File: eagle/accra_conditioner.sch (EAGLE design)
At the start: 25 parts, among them T1 PT204-6C, X1 WIREPAD1,6/0,8, X10 WIREPAD1,6/0,8, X11 WIREPAD1,6/0,8, X12 WIREPAD1,6/0,8, X13 WIREPAD1,6/0,8, X14 WIREPAD1,6/0,8, X15 WIREPAD1,6/0,8, X16 WIREPAD1,6/0,8, X2 WIREPAD1,6/0,8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

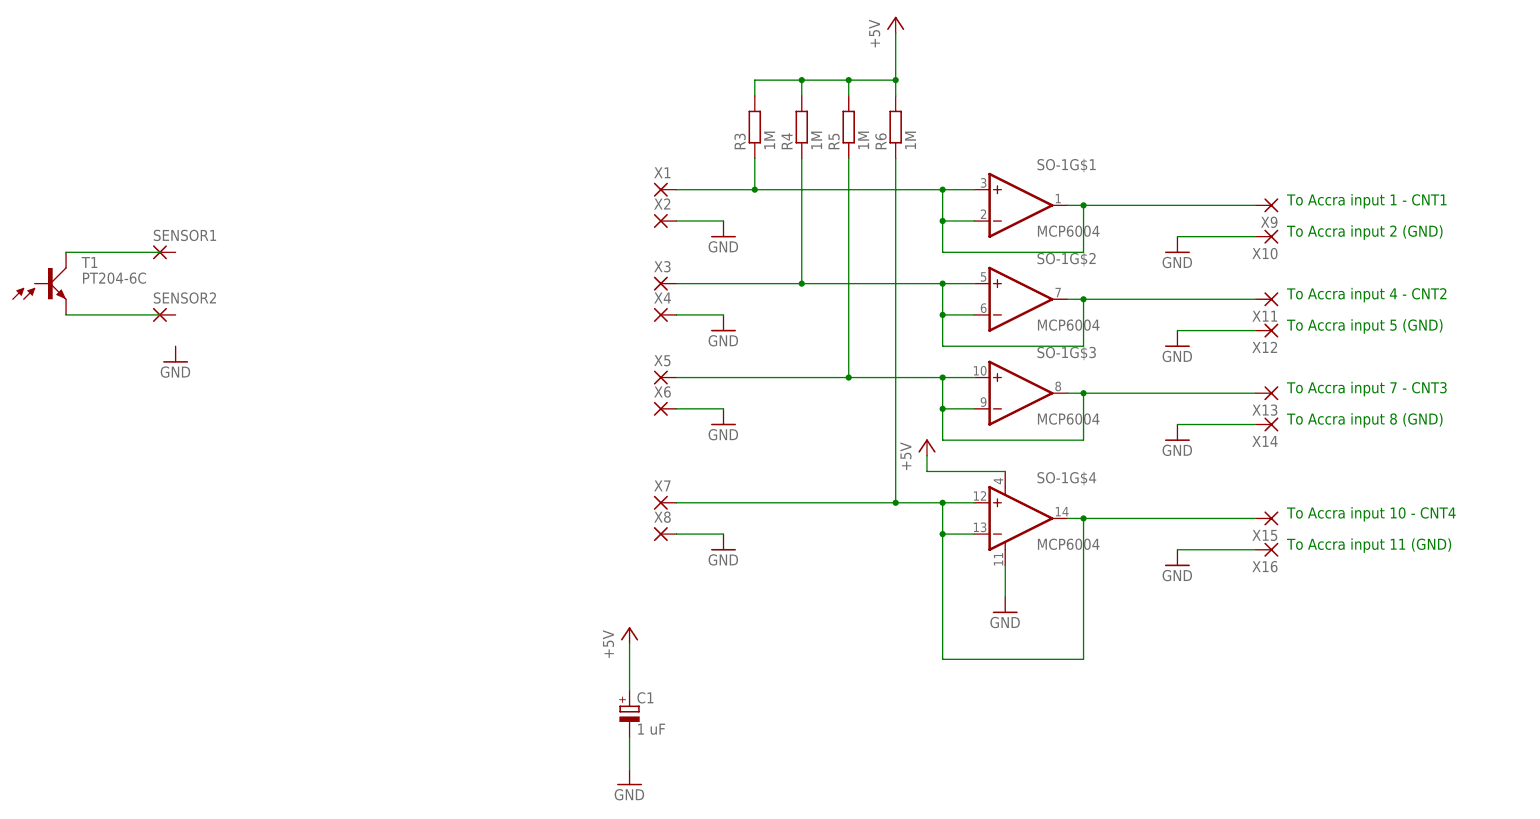
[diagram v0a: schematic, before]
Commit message: Fixed buffer amp.
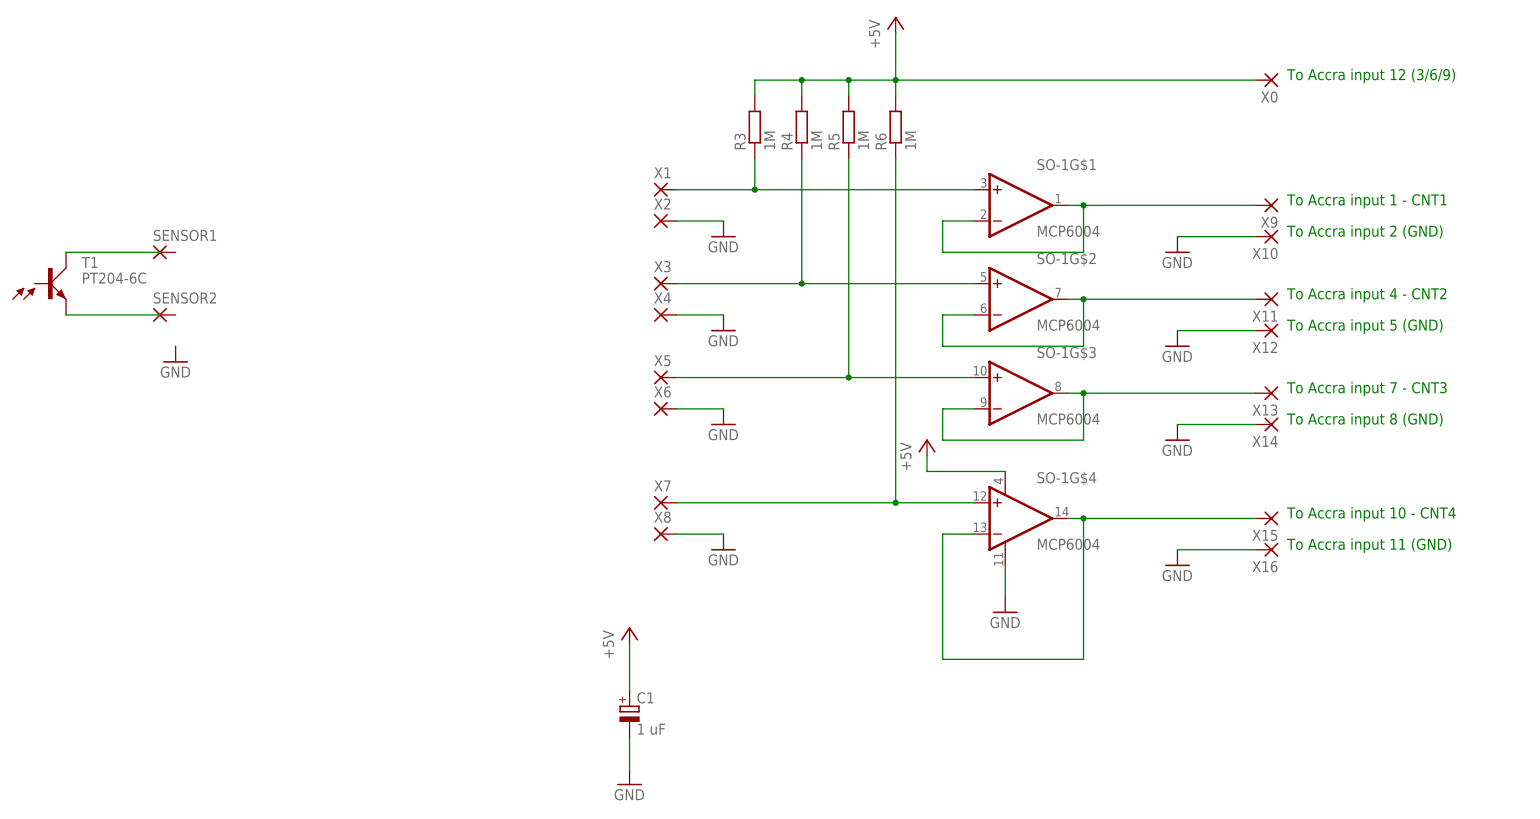
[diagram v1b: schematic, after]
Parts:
- added X0: WIREPAD1,6/0,8, wirepad:WIREPAD1,6/0,8
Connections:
- new net N$10: SO-1G$4.-IN, SO-1G$4.OUT, X15.P
- new net N$2: R3.1, SO-1G$1.+IN, X1.P
- new net N$3: R4.1, SO-1G$2.+IN, X3.P
- new net N$9: SO-1G$3.-IN, SO-1G$3.OUT, X13.P
- net +5V: now also X0.P
- net N$5: no longer R3.1, SO-1G$1.+IN, X1.P
- net N$6: no longer R4.1, SO-1G$2.+IN, X3.P
- net N$7: no longer SO-1G$3.-IN, SO-1G$3.OUT, X13.P
- net N$8: no longer SO-1G$4.-IN, SO-1G$4.OUT, X15.P
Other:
- note added: "To Accra input 12 (3/6/9)"
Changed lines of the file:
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@@
 <part name="X15" library="wirepad" deviceset="WIREPAD" device="1,6/0,8" value=""/>
 <part name="X16" library="wirepad" deviceset="WIREPAD" device="1,6/0,8" value=""/>
+<part name="X0" library="wirepad" deviceset="WIREPAD" device="1,6/0,8" value=""/>
 </parts>
 <sheets>
@@
 <text x="228.6" y="63.5" size="1.778" layer="91">To Accra input 10 - CNT4</text>
 <text x="228.6" y="58.42" size="1.778" layer="91">To Accra input 11 (GND)</text>
+<text x="228.6" y="134.62" size="1.778" layer="91">To Accra input 12 (3/6/9)</text>
 </plain>
 <instances>
@@
 <instance part="X15" gate="G$1" x="226.06" y="63.5" rot="R180"/>
 <instance part="X16" gate="G$1" x="226.06" y="58.42" rot="R180"/>
+<instance part="X0" gate="G$1" x="226.06" y="134.62" rot="R180"/>
 </instances>
 <busses>
@@
 <net name="N$5" class="0">
 <segment>
-<pinref part="SO-1" gate="G$1" pin="+IN"/>
-<wire x1="177.8" y1="116.84" x2="172.72" y2="116.84" width="0.1524" layer="91"/>
-<pinref part="R3" gate="G$1" pin="1"/>
-<wire x1="172.72" y1="116.84" x2="142.24" y2="116.84" width="0.1524" layer="91"/>
-<wire x1="142.24" y1="116.84" x2="129.54" y2="116.84" width="0.1524" layer="91"/>
-<wire x1="142.24" y1="121.92" x2="142.24" y2="116.84" width="0.1524" layer="91"/>
-<junction x="142.24" y="116.84"/>
 <pinref part="SO-1" gate="G$1" pin="-IN"/>
 <wire x1="177.8" y1="111.76" x2="172.72" y2="111.76" width="0.1524" layer="91"/>
-<wire x1="172.72" y1="111.76" x2="172.72" y2="116.84" width="0.1524" layer="91"/>
-<junction x="172.72" y="116.84"/>
 <wire x1="172.72" y1="111.76" x2="172.72" y2="106.68" width="0.1524" layer="91"/>
-<junction x="172.72" y="111.76"/>
 <pinref part="SO-1" gate="G$1" pin="OUT"/>
 <wire x1="193.04" y1="114.3" x2="195.58" y2="114.3" width="0.1524" layer="91"/>
@@
 <wire x1="195.58" y1="106.68" x2="195.58" y2="114.3" width="0.1524" layer="91"/>
 <junction x="195.58" y="114.3"/>
-<pinref part="X1" gate="G$1" pin="P"/>
 <pinref part="X9" gate="G$1" pin="P"/>
 </segment>
@@
 <net name="N$6" class="0">
 <segment>
-<pinref part="SO-1" gate="G$2" pin="+IN"/>
-<wire x1="177.8" y1="101.6" x2="172.72" y2="101.6" width="0.1524" layer="91"/>
 <pinref part="SO-1" gate="G$2" pin="-IN"/>
-<wire x1="172.72" y1="101.6" x2="149.86" y2="101.6" width="0.1524" layer="91"/>
-<wire x1="149.86" y1="101.6" x2="129.54" y2="101.6" width="0.1524" layer="91"/>
 <wire x1="177.8" y1="96.52" x2="172.72" y2="96.52" width="0.1524" layer="91"/>
-<wire x1="172.72" y1="96.52" x2="172.72" y2="101.6" width="0.1524" layer="91"/>
-<junction x="172.72" y="101.6"/>
 <wire x1="172.72" y1="96.52" x2="172.72" y2="91.44" width="0.1524" layer="91"/>
-<junction x="172.72" y="96.52"/>
 <pinref part="SO-1" gate="G$2" pin="OUT"/>
 <wire x1="193.04" y1="99.06" x2="195.58" y2="99.06" width="0.1524" layer="91"/>
@@
 <wire x1="195.58" y1="91.44" x2="195.58" y2="99.06" width="0.1524" layer="91"/>
 <junction x="195.58" y="99.06"/>
-<pinref part="R4" gate="G$1" pin="1"/>
-<wire x1="149.86" y1="121.92" x2="149.86" y2="101.6" width="0.1524" layer="91"/>
-<junction x="149.86" y="101.6"/>
-<pinref part="X3" gate="G$1" pin="P"/>
 <pinref part="X11" gate="G$1" pin="P"/>
 </segment>
@@
 <segment>
 <pinref part="SO-1" gate="G$3" pin="+IN"/>
-<wire x1="177.8" y1="86.36" x2="172.72" y2="86.36" width="0.1524" layer="91"/>
-<pinref part="SO-1" gate="G$3" pin="-IN"/>
-<wire x1="172.72" y1="86.36" x2="157.48" y2="86.36" width="0.1524" layer="91"/>
+<wire x1="177.8" y1="86.36" x2="157.48" y2="86.36" width="0.1524" layer="91"/>
 <wire x1="157.48" y1="86.36" x2="129.54" y2="86.36" width="0.1524" layer="91"/>
-<wire x1="177.8" y1="81.28" x2="172.72" y2="81.28" width="0.1524" layer="91"/>
-<wire x1="172.72" y1="81.28" x2="172.72" y2="86.36" width="0.1524" layer="91"/>
-<junction x="172.72" y="86.36"/>
-<wire x1="172.72" y1="81.28" x2="172.72" y2="76.2" width="0.1524" layer="91"/>
-<junction x="172.72" y="81.28"/>
-<pinref part="SO-1" gate="G$3" pin="OUT"/>
-<wire x1="193.04" y1="83.82" x2="195.58" y2="83.82" width="0.1524" layer="91"/>
-<wire x1="195.58" y1="83.82" x2="223.52" y2="83.82" width="0.1524" layer="91"/>
-<wire x1="172.72" y1="76.2" x2="195.58" y2="76.2" width="0.1524" layer="91"/>
-<wire x1="195.58" y1="76.2" x2="195.58" y2="83.82" width="0.1524" layer="91"/>
-<junction x="195.58" y="83.82"/>
 <pinref part="R5" gate="G$1" pin="1"/>
 <wire x1="157.48" y1="121.92" x2="157.48" y2="86.36" width="0.1524" layer="91"/>
 <junction x="157.48" y="86.36"/>
 <pinref part="X5" gate="G$1" pin="P"/>
-<pinref part="X13" gate="G$1" pin="P"/>
 </segment>
 </net>
@@
 <segment>
 <pinref part="SO-1" gate="G$4" pin="+IN"/>
-<wire x1="177.8" y1="66.04" x2="172.72" y2="66.04" width="0.1524" layer="91"/>
-<pinref part="SO-1" gate="G$4" pin="-IN"/>
-<wire x1="172.72" y1="66.04" x2="165.1" y2="66.04" width="0.1524" layer="91"/>
+<wire x1="177.8" y1="66.04" x2="165.1" y2="66.04" width="0.1524" layer="91"/>
 <wire x1="165.1" y1="66.04" x2="129.54" y2="66.04" width="0.1524" layer="91"/>
-<wire x1="177.8" y1="60.96" x2="172.72" y2="60.96" width="0.1524" layer="91"/>
-<wire x1="172.72" y1="60.96" x2="172.72" y2="66.04" width="0.1524" layer="91"/>
-<junction x="172.72" y="66.04"/>
-<wire x1="172.72" y1="60.96" x2="172.72" y2="40.64" width="0.1524" layer="91"/>
-<junction x="172.72" y="60.96"/>
-<pinref part="SO-1" gate="G$4" pin="OUT"/>
-<wire x1="193.04" y1="63.5" x2="195.58" y2="63.5" width="0.1524" layer="91"/>
-<wire x1="195.58" y1="63.5" x2="223.52" y2="63.5" width="0.1524" layer="91"/>
-<wire x1="172.72" y1="40.64" x2="195.58" y2="40.64" width="0.1524" layer="91"/>
-<wire x1="195.58" y1="40.64" x2="195.58" y2="63.5" width="0.1524" layer="91"/>
-<junction x="195.58" y="63.5"/>
 <pinref part="R6" gate="G$1" pin="1"/>
 <wire x1="165.1" y1="121.92" x2="165.1" y2="66.04" width="0.1524" layer="91"/>
 <junction x="165.1" y="66.04"/>
 <pinref part="X7" gate="G$1" pin="P"/>
-<pinref part="X15" gate="G$1" pin="P"/>
 </segment>
 </net>
@@
 <wire x1="149.86" y1="132.08" x2="149.86" y2="134.62" width="0.1524" layer="91"/>
 <junction x="149.86" y="134.62"/>
-</segment>
-</net>
+<wire x1="165.1" y1="134.62" x2="223.52" y2="134.62" width="0.1524" layer="91"/>
+<pinref part="X0" gate="G$1" pin="P"/>
+</segment>
+</net>
+<net name="N$2" class="0">
+<segment>
+<pinref part="X1" gate="G$1" pin="P"/>
+<pinref part="SO-1" gate="G$1" pin="+IN"/>
+<wire x1="177.8" y1="116.84" x2="142.24" y2="116.84" width="0.1524" layer="91"/>
+<wire x1="142.24" y1="116.84" x2="129.54" y2="116.84" width="0.1524" layer="91"/>
+<pinref part="R3" gate="G$1" pin="1"/>
+<wire x1="142.24" y1="121.92" x2="142.24" y2="116.84" width="0.1524" layer="91"/>
+<junction x="142.24" y="116.84"/>
+</segment>
+</net>
+<net name="N$3" class="0">
+<segment>
+<pinref part="X3" gate="G$1" pin="P"/>
+<pinref part="SO-1" gate="G$2" pin="+IN"/>
+<wire x1="177.8" y1="101.6" x2="149.86" y2="101.6" width="0.1524" layer="91"/>
+<wire x1="149.86" y1="101.6" x2="129.54" y2="101.6" width="0.1524" layer="91"/>
+<junction x="149.86" y="101.6"/>
+<pinref part="R4" gate="G$1" pin="1"/>
+<wire x1="149.86" y1="121.92" x2="149.86" y2="101.6" width="0.1524" layer="91"/>
+</segment>
+</net>
+<net name="N$9" class="0">
+<segment>
+<pinref part="X13" gate="G$1" pin="P"/>
+<pinref part="SO-1" gate="G$3" pin="OUT"/>
+<wire x1="193.04" y1="83.82" x2="195.58" y2="83.82" width="0.1524" layer="91"/>
+<wire x1="195.58" y1="83.82" x2="223.52" y2="83.82" width="0.1524" layer="91"/>
+<junction x="195.58" y="83.82"/>
+<wire x1="195.58" y1="76.2" x2="195.58" y2="83.82" width="0.1524" layer="91"/>
+<wire x1="172.72" y1="76.2" x2="195.58" y2="76.2" width="0.1524" layer="91"/>
+<pinref part="SO-1" gate="G$3" pin="-IN"/>
+<wire x1="177.8" y1="81.28" x2="172.72" y2="81.28" width="0.1524" layer="91"/>
+<wire x1="172.72" y1="81.28" x2="172.72" y2="76.2" width="0.1524" layer="91"/>
+</segment>
+</net>
+<net name="N$10" class="0">
+<segment>
+<pinref part="X15" gate="G$1" pin="P"/>
+<wire x1="195.58" y1="63.5" x2="223.52" y2="63.5" width="0.1524" layer="91"/>
+<pinref part="SO-1" gate="G$4" pin="-IN"/>
+<wire x1="177.8" y1="60.96" x2="172.72" y2="60.96" width="0.1524" layer="91"/>
+<wire x1="172.72" y1="60.96" x2="172.72" y2="40.64" width="0.1524" layer="91"/>
+<wire x1="172.72" y1="40.64" x2="195.58" y2="40.64" width="0.1524" layer="91"/>
+<wire x1="195.58" y1="40.64" x2="195.58" y2="63.5" width="0.1524" layer="91"/>
+<junction x="195.58" y="63.5"/>
+<pinref part="SO-1" gate="G$4" pin="OUT"/>
+<wire x1="193.04" y1="63.5" x2="195.58" y2="63.5" width="0.1524" layer="91"/>
+</segment>
+</net>
